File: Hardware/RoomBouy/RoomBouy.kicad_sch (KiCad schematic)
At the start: 0 parts

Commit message: Add upstream libs and kicad templates
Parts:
- added J2: Raspberry_Pi_2_3, RPI_Hat:RPI_Hat_B+, symbol Connector:Raspberry_Pi_2_3
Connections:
- new net: J2.1 (3V3), J2.17 (3V3)
- new net: J2.14 (GND), J2.20 (GND), J2.25 (GND), J2.30 (GND), J2.34 (GND), J2.39 (GND), J2.6 (GND), J2.9 (GND)
- new net: J2.2 (5V), J2.4 (5V)
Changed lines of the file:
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@@
-(kicad_sch (version 20230121) (generator eeschema)
-  (paper "A4")
-  (title_block
-    (title "RoomBouy")
-    (rev "${REVISION}")
-    (company "Concord Robotics")
-  )
-  (sheet_instances
-    (path "/" (page "1"))
-  )
+(kicad_sch
+	(version 20231120)
+	(generator "eeschema")
+	(generator_version "8.0")
+	(paper "A4")
+	(title_block
+		(title "RoomBouy")
+		(rev "${REVISION}")
+		(company "Concord Robotics")
+	)
+	(symbol
+		(lib_id "Connector:Raspberry_Pi_2_3")
+		(at 144.78 95.25 0)
+		(unit 1)
+		(exclude_from_sim no)
+		(in_bom yes)
+		(on_board yes)
+		(dnp no)
+		(fields_autoplaced yes)
+		(property "Reference" "J2"
+			(at 146.9741 128.27 0)
+			(effects
+				(font
+					(size 1.27 1.27)
+				)
+				(justify left)
+			)
+		)
+		(property "Value" "Raspberry_Pi_2_3"
+			(at 146.9741 130.81 0)
+			(effects
+				(font
+					(size 1.27 1.27)
+				)
+				(justify left)
+			)
+		)
+		(property "Footprint" "RPI_Hat:RPI_Hat_B+"
+			(at 144.78 95.25 0)
+			(effects
+				(font
+					(size 1.27 1.27)
+				)
+				(hide yes)
+			)
+		)
+		(property "Datasheet" "https://www.raspberrypi.org/documentation/hardware/raspberrypi/schematics/rpi_SCH_3bplus_1p0_reduced.pdf"
+			(at 205.74 139.7 0)
+			(effects
+				(font
+					(size 1.27 1.27)
+				)
+				(hide yes)
+			)
+		)
+		(property "Description" "expansion header for Raspberry Pi 2 & 3"
+			(at 144.78 95.25 0)
+			(effects
+				(font
+					(size 1.27 1.27)
+				)
+				(hide yes)
+			)
+		)
+		(pin "33"
+		)
+		(pin "35"
+		)
+		(pin "40"
+		)
+		(pin "38"
+		)
+		(pin "27"
+		)
+		(pin "37"
+		)
+		(pin "5"
+		)
+		(pin "34"
+		)
+		(pin "15"
+		)
+		(pin "39"
+		)
+		(pin "1"
+		)
+		(pin "23"
+		)
+		(pin "9"
+		)
+		(pin "12"
+		)
+		(pin "19"
+		)
+		(pin "2"
+		)
+		(pin "8"
+		)
+		(pin "3"
+		)
+		(pin "30"
+		)
+		(pin "31"
+		)
+		(pin "24"
+		)
+		(pin "18"
+		)
+		(pin "14"
+		)
+		(pin "21"
+		)
+		(pin "13"
+		)
+		(pin "22"
+		)
+		(pin "17"
+		)
+		(pin "25"
+		)
+		(pin "11"
+		)
+		(pin "28"
+		)
+		(pin "7"
+		)
+		(pin "20"
+		)
+		(pin "36"
+		)
+		(pin "26"
+		)
+		(pin "4"
+		)
+		(pin "10"
+		)
+		(pin "6"
+		)
+		(pin "32"
+		)
+		(pin "16"
+		)
+		(pin "29"
+		)
+		(instances
+			(project ""
+				(path "/894f620e-3404-4a40-a2a7-513bc1d5f99b"
+					(reference "J2")
+					(unit 1)
+				)
+			)
+		)
+	)
+	(sheet_instances
+		(path "/"
+			(page "1")
+		)
+	)
 )

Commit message: Clean sheet
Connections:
- net GND: now reaches J2.14 (GND), J2.20 (GND), J2.25 (GND), J2.30 (GND), J2.34 (GND), J2.39 (GND), J2.6 (GND), J2.9 (GND)
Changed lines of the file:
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@@
 		(company "Concord Robotics")
+	)
+	(wire
+		(pts
+			(xy 144.78 128.27) (xy 144.78 130.81)
+		)
+		(stroke
+			(width 0)
+			(type default)
+		)
+	)
+	(symbol
+		(lib_id "power:GND")
+		(at 144.78 130.81 0)
+		(unit 1)
+		(exclude_from_sim no)
+		(in_bom yes)
+		(on_board yes)
+		(dnp no)
+		(property "Reference" "#PWR01"
+			(at 144.78 137.16 0)
+			(effects
+				(font
+					(size 1.27 1.27)
+				)
+				(hide yes)
+			)
+		)
+		(property "Value" "GND"
+			(at 144.78 134.874 0)
+			(effects
+				(font
+					(size 1.27 1.27)
+				)
+			)
+		)
+		(property "Footprint" ""
+			(at 144.78 130.81 0)
+			(effects
+				(font
+					(size 1.27 1.27)
+				)
+				(hide yes)
+			)
+		)
+		(property "Datasheet" ""
+			(at 144.78 130.81 0)
+			(effects
+				(font
+					(size 1.27 1.27)
+				)
+				(hide yes)
+			)
+		)
+		(property "Description" "Power symbol creates a global label with name \"GND\" , ground"
+			(at 144.78 130.81 0)
+			(effects
+				(font
+					(size 1.27 1.27)
+				)
+				(hide yes)
+			)
+		)
+		(pin "1"
+		)
+		(instances
+			(project ""
+				(path "/894f620e-3404-4a40-a2a7-513bc1d5f99b"
+					(reference "#PWR01")
+					(unit 1)
+				)
+			)
+		)
 	)
 	(symbol
@@
 		(on_board yes)
 		(dnp no)
-		(fields_autoplaced yes)
 		(property "Reference" "J2"
-			(at 146.9741 128.27 0)
+			(at 163.576 122.174 0)
 			(effects
 				(font
@@
 		)
 		(property "Value" "Raspberry_Pi_2_3"
-			(at 146.9741 130.81 0)
+			(at 163.576 124.714 0)
 			(effects
 				(font

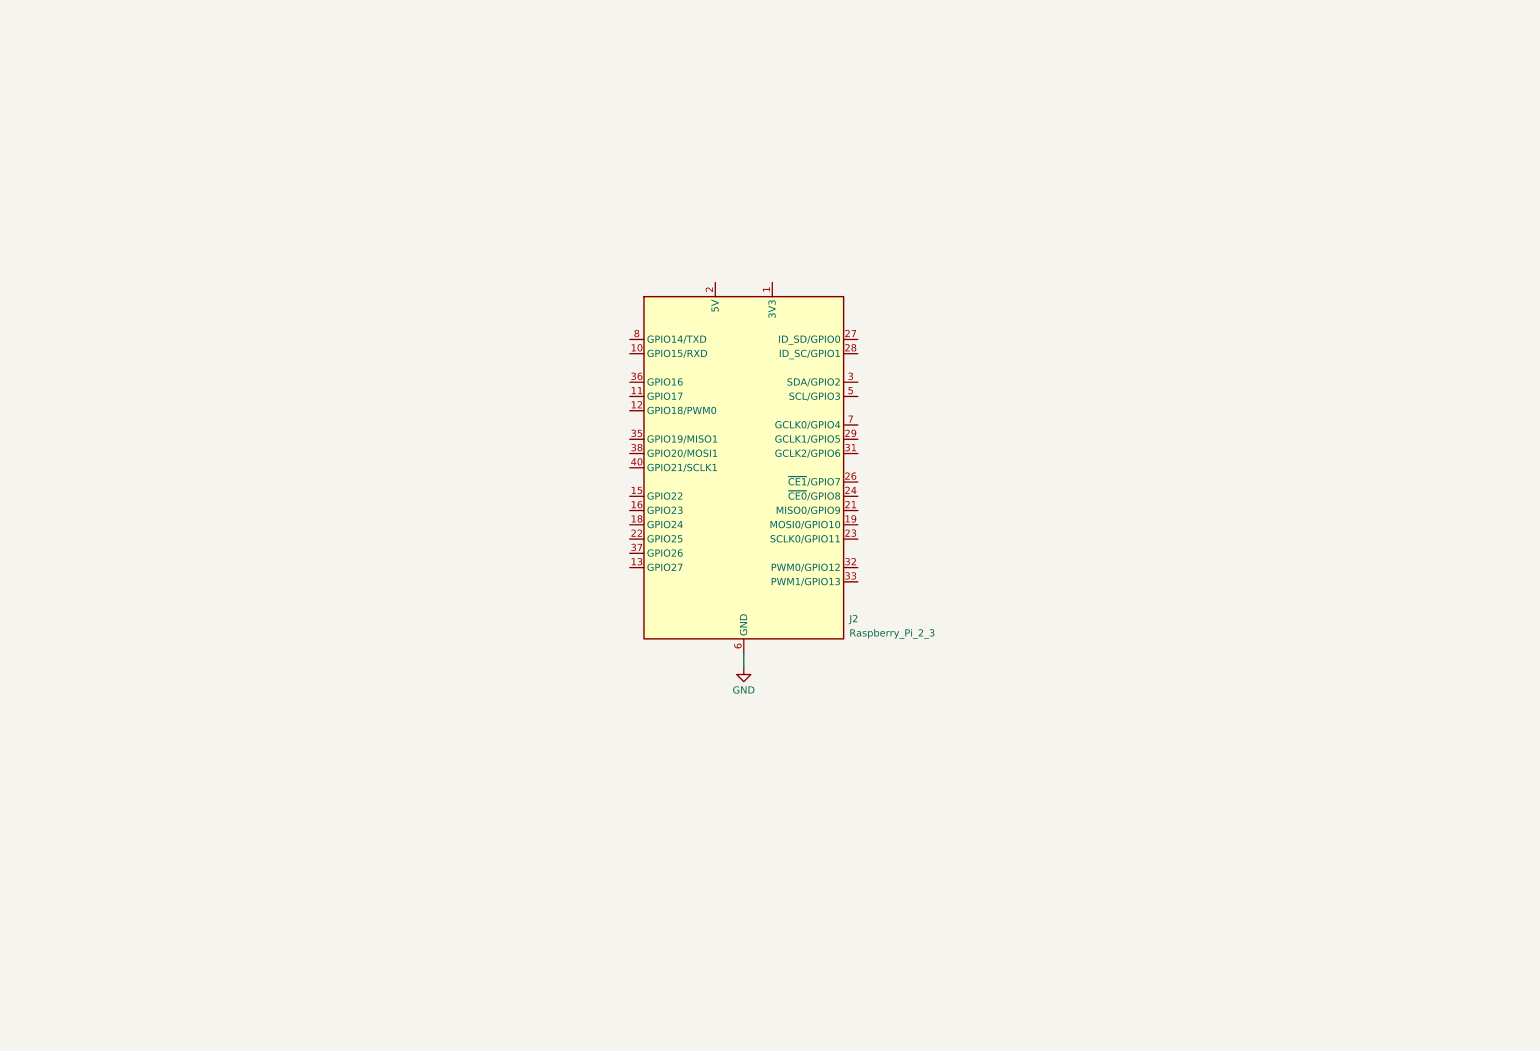
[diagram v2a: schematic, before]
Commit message: Add internal libs, do full board layout, bump k8 and fix ERC
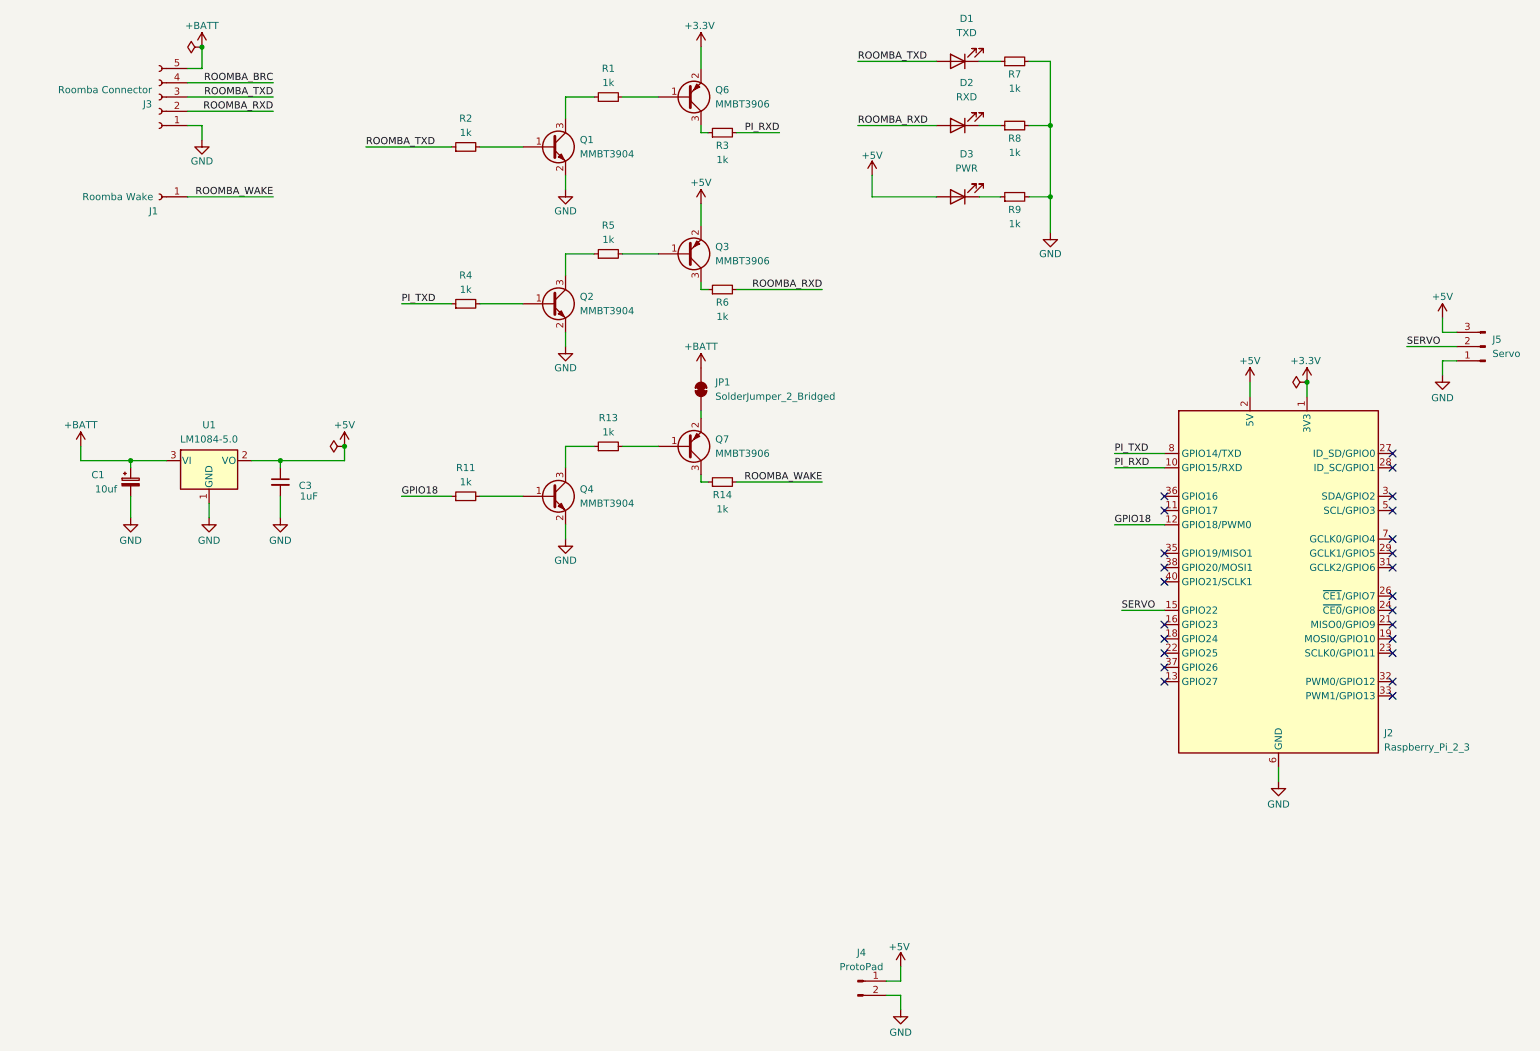
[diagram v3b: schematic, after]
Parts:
- added C1: 10uf, Capacitor_SMD:CP_Elec_4x3, symbol Device:C_Polarized_Small
- added C3: 1uF, Capacitor_SMD:C_0805_2012Metric, symbol Device:C_Small
- added D1: TXD, LED_SMD:LED_0805_2012Metric, symbol Device:LED
- added D2: RXD, LED_SMD:LED_0805_2012Metric, symbol Device:LED
- added D3: PWR, LED_SMD:LED_0805_2012Metric, symbol Device:LED
- added J1: Roomba Wake, Connector_Wire:SolderWire-0.25sqmm_1x01_D0.65mm_OD1.7mm_Relief, symbol Connector:Conn_01x01_Socket
- added J3: Roomba Connector, Connector_Wire:SolderWire-0.25sqmm_1x05_P4.2mm_D0.65mm_OD1.7mm_Relief, symbol Connector:Conn_01x05_Socket
- added J4: ProtoPad, RoomBouy:ProtoPad, symbol Connector:Conn_01x02_Pin
- added J5: Servo, Connector_JST:JST_PH_S3B-PH-K_1x03_P2.00mm_Horizontal, symbol Connector:Conn_01x03_Pin
- added JP1: SolderJumper_2_Bridged, Jumper:SolderJumper-2_P1.3mm_Bridged2Bar_RoundedPad1.0x1.5mm, symbol Jumper:SolderJumper_2_Bridged
- added Q1, Q2, Q4: MMBT3904, Package_TO_SOT_SMD:SOT-23, symbol Transistor_BJT:MMBT3904
- added Q3, Q6, Q7: MMBT3906, Package_TO_SOT_SMD:SOT-23, symbol Transistor_BJT:MMBT3906
- added R1, R11, R13, R14, R2, R3, R4, R5, R6, R7, R8, R9: 1k, Resistor_SMD:R_0805_2012Metric, symbol Device:R_Small
- added U1: LM1084-5.0, Package_TO_SOT_THT:TO-220-3_Horizontal_TabDown, symbol Regulator_Linear:LM1084-5.0
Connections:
- net GND: now also C1.2, C3.2, J3.1 (Pin_1), J4.2 (Pin_2), J5.1 (Pin_1), Q1.2 (E), Q2.2 (E), Q4.2 (E), R7.2, R8.2, R9.2, U1.1 (GND)
- net +3.3V: now reaches J2.1 (3V3), J2.17 (3V3)
- net +3.3V: now also Q6.2 (E)
- net PI_RXD: now reaches J2.10 (GPIO15/RXD)
- net PI_RXD: now also R3.2
- net GPIO18: now reaches J2.12 (GPIO18/PWM0)
- net GPIO18: now also R11.1
- net SERVO: now reaches J2.15 (GPIO22)
- net SERVO: now also J5.2 (Pin_2)
- net +5V: now reaches J2.2 (5V), J2.4 (5V)
- net +5V: now also C3.1, D3.2 (A), J4.1 (Pin_1), J5.3 (Pin_3), Q3.2 (E), U1.2 (VO)
- net PI_TXD: now reaches J2.8 (GPIO14/TXD)
- net PI_TXD: now also R4.1
- new net: D2.1 (K), R8.1
- new net: Q4.1 (B), R11.2
- new net: Q4.3 (C), R13.1
- new net: Q7.3 (C), R14.1
- new net: D3.1 (K), R9.1
- new net: JP1.1 (A), Q7.2 (E)
- new net: Q1.3 (C), R1.1
- new net: Q6.1 (B), R1.2
- new net: Q7.1 (B), R13.2
- new net: Q1.1 (B), R2.2
- new net: Q2.1 (B), R4.2
- new net: Q2.3 (C), R5.1
- new net: Q3.1 (B), R5.2
- new net: Q3.3 (C), R6.1
- new net: Q6.3 (C), R3.1
- new net: D1.1 (K), R7.1
- new net +BATT: C1.1, J3.5 (Pin_5), JP1.2 (B), U1.3 (VI)
- new net ROOMBA_BRC: J3.4 (Pin_4)
- new net ROOMBA_RXD: D2.2 (A), J3.2 (Pin_2), R6.2
- new net ROOMBA_TXD: D1.2 (A), J3.3 (Pin_3), R2.1
- new net ROOMBA_WAKE: J1.1 (Pin_1), R14.2
- no-connect marks 0 -> 24
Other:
- moved on the sheet: J2

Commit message: Fix DRC
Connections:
- net ROOMBA_BRC: no longer names the net of J3.4 (Pin_4)
- no-connect marks 24 -> 25
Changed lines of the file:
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@@
 	)
 	(junction
-		(at 48.26 20.32)
+		(at 48.26 36.83)
 		(diameter 0)
 		(color 0 0 0 0)
 	)
 	(junction
-		(at 73.66 91.44)
+		(at 48.26 20.32)
 		(diameter 0)
 		(color 0 0 0 0)
@@
 	)
 	(no_connect
+		(at 60.96 26.67)
+	)
+	(no_connect
 		(at 219.71 110.49)
 	)
@@
 		)
 	)
-	(label "ROOMBA_BRC"
-		(at 60.96 26.67 180)
-		(fields_autoplaced yes)
-		(effects
-			(font
-				(size 1.27 1.27)
-			)
-			(justify right bottom)
-		)
-	)
 	(label "ROOMBA_WAKE"
 		(at 158.75 97.79 180)
@@
 			)
 		)
-		(property "Datasheet" "https://www.onsemi.com/pub/Collateral/2N3903-D.PDF"
+		(property "Datasheet" "https://www.onsemi.com/pdf/datasheet/pzt3904-d.pdf"
 			(at 110.49 100.33 0)
 			(effects
@@
 			)
 		)
-		(property "Description" ""
+		(property "Description" "0.2A Ic, 40V Vce, Small Signal NPN Transistor, SOT-23"
 			(at 110.49 100.33 0)
 			(effects
@@
 			)
 		)
-		(property "Datasheet" "https://www.onsemi.com/pub/Collateral/2N3906-D.PDF"
+		(property "Datasheet" "https://www.onsemi.com/pdf/datasheet/pzt3906-d.pdf"
 			(at 134.62 91.44 0)
 			(effects
@@
 			)
 		)
-		(property "Description" ""
+		(property "Description" "-0.2A Ic, -40V Vce, Small Signal PNP Transistor, SOT-23"
 			(at 134.62 91.44 0)
 			(effects
@@
 	)
 	(symbol
+		(lib_name "MMBT3904_1")
 		(lib_id "Transistor_BJT:MMBT3904")
 		(at 110.49 38.1 0)
@@
 			)
 		)
-		(property "Datasheet" "https://www.onsemi.com/pub/Collateral/2N3903-D.PDF"
+		(property "Datasheet" "https://www.onsemi.com/pdf/datasheet/pzt3904-d.pdf"
 			(at 110.49 38.1 0)
 			(effects
@@
 			)
 		)
-		(property "Description" ""
+		(property "Description" "0.2A Ic, 40V Vce, Small Signal NPN Transistor, SOT-23"
 			(at 110.49 38.1 0)
 			(effects
@@
 	)
 	(symbol
+		(lib_name "MMBT3904_2")
 		(lib_id "Transistor_BJT:MMBT3904")
 		(at 110.49 66.04 0)
@@
 			)
 		)
-		(property "Datasheet" "https://www.onsemi.com/pub/Collateral/2N3903-D.PDF"
+		(property "Datasheet" "https://www.onsemi.com/pdf/datasheet/pzt3904-d.pdf"
 			(at 110.49 66.04 0)
 			(effects
@@
 			)
 		)
-		(property "Description" ""
+		(property "Description" "0.2A Ic, 40V Vce, Small Signal NPN Transistor, SOT-23"
 			(at 110.49 66.04 0)
 			(effects
@@
 	)
 	(symbol
+		(lib_name "MMBT3906_2")
 		(lib_id "Transistor_BJT:MMBT3906")
 		(at 134.62 57.15 0)
@@
 			)
 		)
-		(property "Datasheet" "https://www.onsemi.com/pub/Collateral/2N3906-D.PDF"
+		(property "Datasheet" "https://www.onsemi.com/pdf/datasheet/pzt3906-d.pdf"
 			(at 134.62 57.15 0)
 			(effects
@@
 			)
 		)
-		(property "Description" ""
+		(property "Description" "-0.2A Ic, -40V Vce, Small Signal PNP Transistor, SOT-23"
 			(at 134.62 57.15 0)
 			(effects
@@
 	)
 	(symbol
+		(lib_name "MMBT3906_1")
 		(lib_id "Transistor_BJT:MMBT3906")
 		(at 134.62 29.21 0)
@@
 			)
 		)
-		(property "Datasheet" "https://www.onsemi.com/pub/Collateral/2N3906-D.PDF"
+		(property "Datasheet" "https://www.onsemi.com/pdf/datasheet/pzt3906-d.pdf"
 			(at 134.62 29.21 0)
 			(effects
@@
 			)
 		)
-		(property "Description" ""
+		(property "Description" "-0.2A Ic, -40V Vce, Small Signal PNP Transistor, SOT-23"
 			(at 134.62 29.21 0)
 			(effects
@@
 	(symbol
 		(lib_id "power:PWR_FLAG")
-		(at 73.66 91.44 90)
+		(at 48.26 36.83 90)
 		(unit 1)
 		(exclude_from_sim no)
@@
 		(dnp no)
 		(fields_autoplaced yes)
-		(property "Reference" "#FLG03"
-			(at 71.755 91.44 0)
+		(property "Reference" "#FLG04"
+			(at 46.355 36.83 0)
 			(effects
 				(font
@@
 		)
 		(property "Value" "PWR_FLAG"
-			(at 69.85 91.4399 90)
+			(at 44.45 36.8299 90)
 			(effects
 				(font
@@
 		)
 		(property "Footprint" ""
-			(at 73.66 91.44 0)
+			(at 48.26 36.83 0)
 			(effects
 				(font
@@
 		)
 		(property "Datasheet" "~"
-			(at 73.66 91.44 0)
+			(at 48.26 36.83 0)
 			(effects
 				(font
@@
 		)
 		(property "Description" "Special symbol for telling ERC where power comes from"
-			(at 73.66 91.44 0)
+			(at 48.26 36.83 0)
 			(effects
 				(font
@@
 			(project "RoomBouy"
 				(path "/894f620e-3404-4a40-a2a7-513bc1d5f99b"
-					(reference "#FLG03")
+					(reference "#FLG04")
 					(unit 1)
 				)
